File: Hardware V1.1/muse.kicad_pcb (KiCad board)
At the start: 2 copper layers, 71.6 x 61.5 mm, 53 parts, among them P1 3.5mm_line, P2 3.5mm_line, P3 RCA, P4 RCA, P8 ATX_PS_ON, P9 LED_Signal, Q1 FQP30N06L, Q2 FQP30N06L, Q3 FQP30N06L, Q4 FQP30N06L, Q5 FQP30N06L, Q6 FQP30N06L, SW1 PWR_SW, U1 MSGEQ7, U2 MSGEQ7, U3 74LS595, U4 Spark_Core

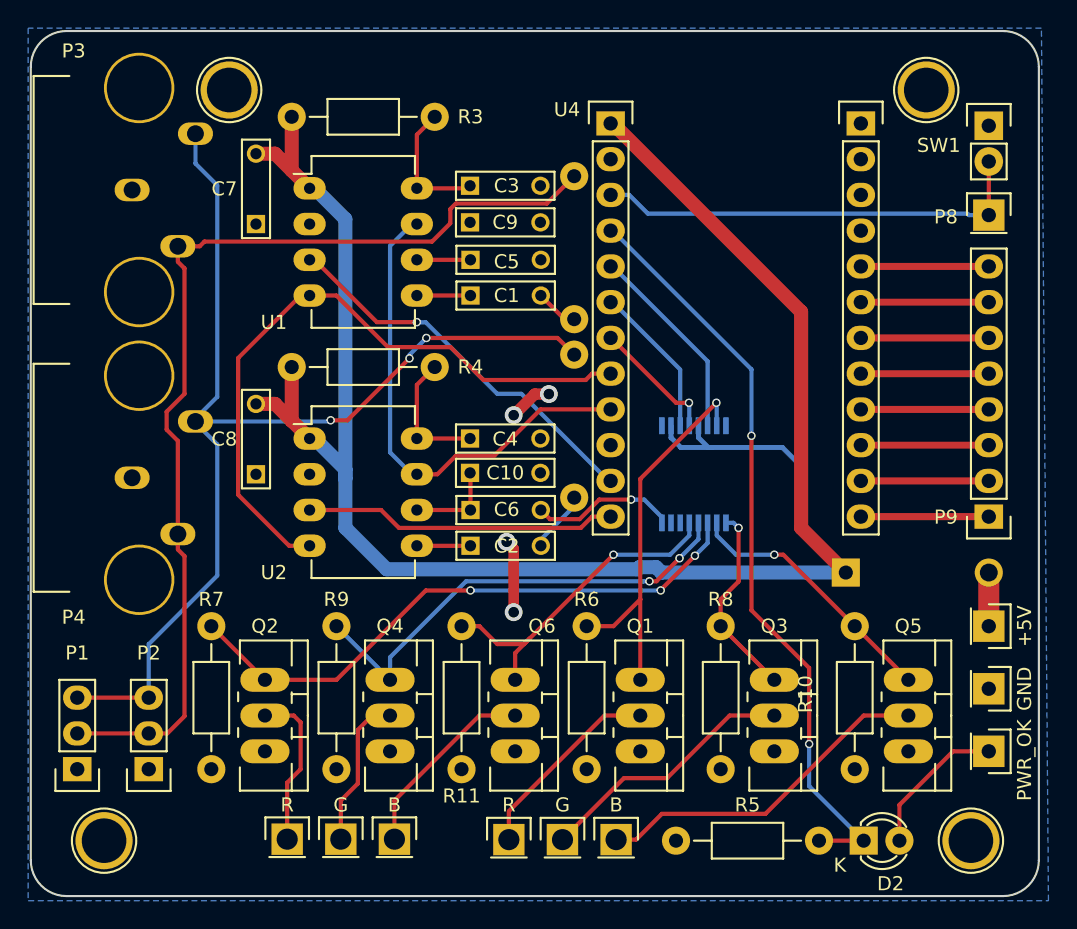
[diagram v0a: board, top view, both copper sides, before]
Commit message: Changed versioning scheme. Fixed problems and reuploaded to oshpark
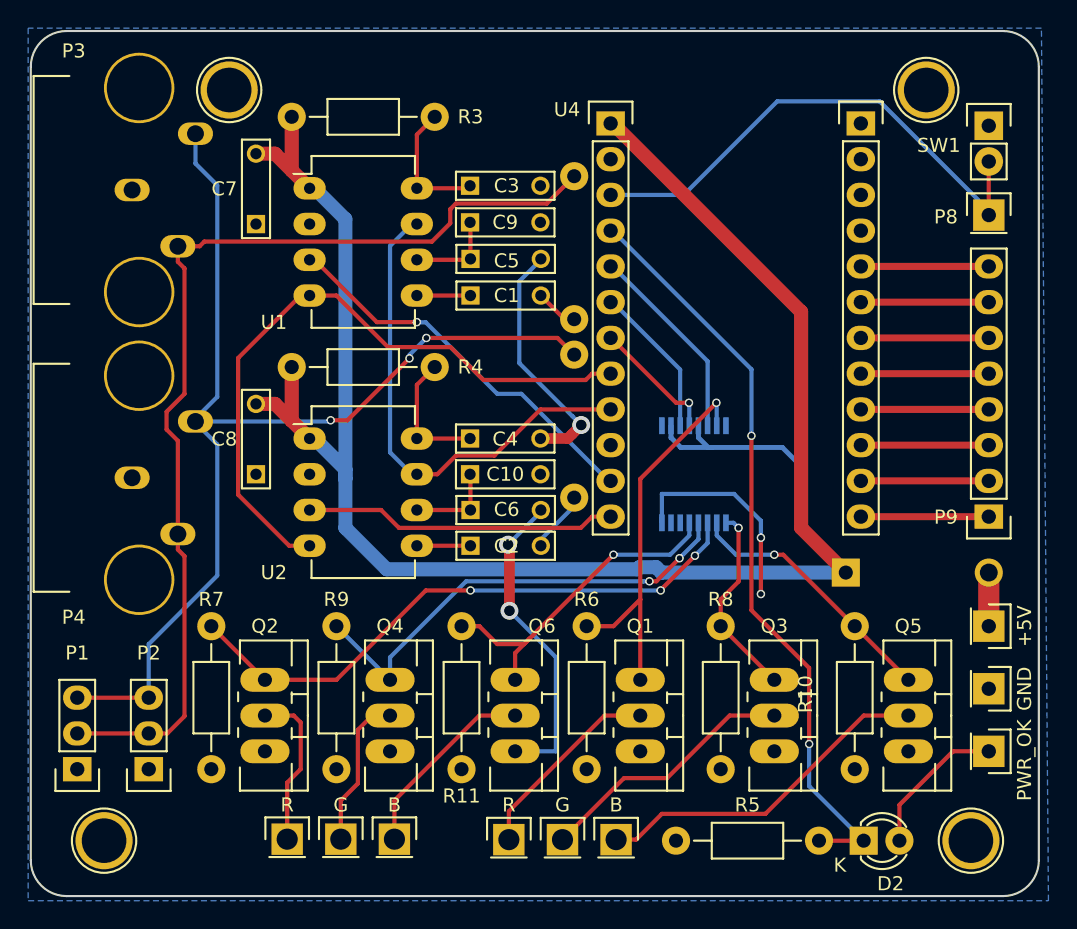
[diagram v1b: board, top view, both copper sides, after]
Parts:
- moved C10 0.10 mm to (114.9, 102.2)
- moved C5 0.06 mm to (114.9, 86.9)
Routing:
- net GND: track 10.4 -> 55.4 mm, vias 1 -> 5
- net (no net): track 8.33 -> 0.00 mm, vias 4 -> 0
- net /ATX_PWR_ON: track 27.5 -> 33.2 mm
- net Net-(C5-Pad1): track 3.81 -> 6.48 mm
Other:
- board text added: "(1.1)"
- board text removed: "(2.0)"
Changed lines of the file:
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@@
   (general
     (links 100)
-    (no_connects 3)
-    (area 82.434286 70.663999 156.111429 133.055)
+    (no_connects 1)
+    (area 82.434286 70.535 156.111429 133.055)
     (thickness 1.6)
     (drawings 11)
-    (tracks 275)
+    (tracks 285)
     (zones 0)
     (modules 53)
@@
     (aux_axis_origin 0 0)
     (grid_origin 103.505 89.535)
-    (visible_elements FFFFFF7F)
+    (visible_elements 7FFFFFFF)
     (pcbplotparams
-      (layerselection 0x00030_80000001)
+      (layerselection 0x010f0_80000001)
       (usegerberextensions false)
       (excludeedgelayer true)
@@
       (outputformat 1)
       (mirror false)
-      (drillshape 1)
+      (drillshape 0)
       (scaleselection 1)
-      (outputdirectory ""))
+      (outputdirectory Gerbers/))
   )
   (net 0 "")
@@
   )
   (module Capacitors_ThroughHole:C_Rect_L7_W2_P5 (layer F.Cu)
-    (at 114.935 86.995)
+    (at 114.935 86.9315)
     (descr "Film Capacitor Length 7 x Width 2mm, Pitch 5mm")
     (tags Capacitor)
@@
     (descr "Resistor, Axial,  RM 10mm, 1/3W,")
     (tags "Resistor, Axial, RM 10mm, 1/3W,")
-    (fp_text reference R1 (at 0 2.54 90) (layer B.SilkS)
+    (fp_text reference R1 (at 8.03 -0.1945 90) (layer B.SilkS)
       (effects (font (size 1 1) (thickness 0.15)) (justify mirror))
     )
@@
     (descr "Resistor, Axial,  RM 10mm, 1/3W,")
     (tags "Resistor, Axial, RM 10mm, 1/3W,")
-    (fp_text reference R2 (at 0 2.54 270) (layer B.SilkS)
+    (fp_text reference R2 (at 7.611 0.004 270) (layer B.SilkS)
       (effects (font (size 1 1) (thickness 0.15)) (justify mirror))
     )
@@
   )
   (module Capacitors_ThroughHole:C_Rect_L7_W2_P5 (layer F.Cu)
-    (at 114.905 102.135)
+    (at 114.905 102.235)
     (descr "Film Capacitor Length 7 x Width 2mm, Pitch 5mm")
     (tags Capacitor)
@@
     )
   )
-  (gr_text "(2.0)" (at 145.923 94.234 90) (layer B.SilkS)
+  (gr_text "(1.1)" (at 145.923 94.234 90) (layer B.SilkS)
     (effects (font (size 1 1) (thickness 0.2)) (justify left mirror))
   )
@@
   (gr_line (start 155.321 73.279) (end 155.321 129.667) (layer Edge.Cuts) (width 0.15))
   (gr_line (start 86.233 70.739) (end 152.781 70.739) (layer Edge.Cuts) (width 0.15))
-  (segment (start 118.005 112.035) (end 118.005 107.535) (width 0.762) (layer F.Cu) (net 0))
-  (via (at 117.505 107.035) (size 1.27) (drill 0.762) (layers F.Cu B.Cu) (net 0))
-  (segment (start 118.005 107.535) (end 117.505 107.035) (width 0.762) (layer F.Cu) (net 0))
-  (via (at 118.005 112.035) (size 1.27) (drill 0.762) (layers F.Cu B.Cu) (net 0))
-  (segment (start 118.005 98.035) (end 119.505 96.535) (width 0.808) (layer F.Cu) (net 0))
-  (segment (start 119.505 96.535) (end 120.505 96.535) (width 0.808) (layer F.Cu) (net 0))
-  (via (at 120.505 96.535) (size 1.27) (drill 0.762) (layers F.Cu B.Cu) (net 0))
-  (via (at 118.005 98.035) (size 1.27) (drill 0.762) (layers F.Cu B.Cu) (net 0))
   (segment (start 114.935 89.535) (end 111.125 89.535) (width 0.3) (layer F.Cu) (net 1) (status 30))
   (segment (start 119.935 89.535) (end 121.615 91.215) (width 0.3) (layer F.Cu) (net 2))
@@
   (segment (start 111.125 78.105) (end 112.395 76.835) (width 0.3) (layer F.Cu) (net 5) (status 20))
   (segment (start 111.125 81.915) (end 111.125 78.105) (width 0.3) (layer F.Cu) (net 5) (status 10))
-  (segment (start 126.34999 104.035) (end 127.285 104.035) (width 0.3) (layer B.Cu) (net 6))
-  (segment (start 127.285 104.035) (end 128.535 105.285) (width 0.3) (layer B.Cu) (net 6))
+  (segment (start 128.535 105.685) (end 128.535 103.632) (width 0.3) (layer B.Cu) (net 6))
+  (segment (start 128.535 103.632) (end 133.6675 103.632) (width 0.3) (layer B.Cu) (net 6))
+  (segment (start 133.6675 103.632) (end 135.5725 105.537) (width 0.3) (layer B.Cu) (net 6))
+  (segment (start 135.5725 105.537) (end 135.5725 106.7435) (width 0.3) (layer B.Cu) (net 6))
+  (segment (start 135.5725 106.7435) (end 135.5725 110.744) (width 0.3) (layer F.Cu) (net 6))
+  (via (at 135.5725 110.744) (size 0.6) (drill 0.4) (layers F.Cu B.Cu) (net 6))
+  (via (at 135.5725 106.7435) (size 0.6) (drill 0.4) (layers F.Cu B.Cu) (net 6))
+  (segment (start 119.905 99.695) (end 121.845 99.695) (width 0.762) (layer F.Cu) (net 6))
+  (segment (start 122.170001 99.369999) (end 122.805 98.735) (width 0.762) (layer F.Cu) (net 6))
+  (segment (start 122.170001 98.100001) (end 122.805 98.735) (width 0.3) (layer B.Cu) (net 6))
+  (segment (start 121.845 99.695) (end 122.170001 99.369999) (width 0.762) (layer F.Cu) (net 6))
+  (segment (start 118.405 94.335) (end 122.170001 98.100001) (width 0.3) (layer B.Cu) (net 6))
+  (segment (start 118.405 88.525) (end 118.405 94.335) (width 0.3) (layer B.Cu) (net 6))
+  (segment (start 119.935 86.995) (end 118.405 88.525) (width 0.3) (layer B.Cu) (net 6))
+  (via (at 122.805 98.735) (size 1.27) (drill 0.762) (layers F.Cu B.Cu) (net 6))
+  (segment (start 118.11 121.92) (end 121.005 121.92) (width 0.3) (layer B.Cu) (net 6))
+  (segment (start 121.005 121.92) (end 121.005 115.235) (width 0.3) (layer B.Cu) (net 6))
+  (segment (start 121.005 115.235) (end 117.705 111.935) (width 0.3) (layer B.Cu) (net 6))
+  (segment (start 117.605 107.235) (end 119.935 104.905) (width 0.3) (layer B.Cu) (net 6))
+  (segment (start 119.935 104.905) (end 119.935 104.775) (width 0.3) (layer B.Cu) (net 6))
+  (segment (start 117.705 111.935) (end 117.705 107.335) (width 0.762) (layer F.Cu) (net 6))
+  (segment (start 117.705 107.335) (end 117.605 107.235) (width 0.762) (layer F.Cu) (net 6))
+  (via (at 117.605 107.235) (size 1.27) (drill 0.762) (layers F.Cu B.Cu) (net 6))
+  (via (at 117.705 111.935) (size 1.27) (drill 0.762) (layers F.Cu B.Cu) (net 6))
   (segment (start 128.535 105.285) (end 128.535 105.685) (width 0.3) (layer B.Cu) (net 6))
-  (segment (start 119.935 104.775) (end 120.584999 105.424999) (width 0.3) (layer F.Cu) (net 6))
-  (segment (start 120.584999 105.424999) (end 122.691971 105.424999) (width 0.3) (layer F.Cu) (net 6))
-  (segment (start 122.691971 105.424999) (end 124.084852 104.032118) (width 0.3) (layer F.Cu) (net 6))
-  (segment (start 124.084852 104.032118) (end 126.347108 104.032118) (width 0.3) (layer F.Cu) (net 6))
-  (segment (start 126.347108 104.032118) (end 126.34999 104.035) (width 0.3) (layer F.Cu) (net 6))
-  (via (at 126.34999 104.035) (size 0.6) (drill 0.4) (layers F.Cu B.Cu) (net 6))
   (segment (start 111.125 99.695) (end 115.015 99.695) (width 0.3) (layer F.Cu) (net 7) (status 30))
   (segment (start 111.125 95.885) (end 112.395 94.615) (width 0.3) (layer F.Cu) (net 7) (status 20))
   (segment (start 111.125 99.695) (end 111.125 95.885) (width 0.3) (layer F.Cu) (net 7) (status 10))
+  (segment (start 114.935 86.995) (end 114.935 84.365) (width 0.3) (layer F.Cu) (net 8))
+  (segment (start 114.935 84.365) (end 114.905 84.335) (width 0.3) (layer F.Cu) (net 8))
   (segment (start 114.935 86.995) (end 111.125 86.995) (width 0.3) (layer F.Cu) (net 8) (status 30))
   (segment (start 103.855 99.695) (end 103.505 99.695) (width 1) (layer F.Cu) (net 9) (status 30))
@@
   (segment (start 134.9 94.778966) (end 134.9 99.5) (width 0.3) (layer B.Cu) (net 43))
   (via (at 134.9 99.5) (size 0.6) (drill 0.4) (layers F.Cu B.Cu) (net 43))
-  (segment (start 124.894362 82.385728) (end 126.210362 82.385728) (width 0.3) (layer B.Cu) (net 44))
-  (segment (start 126.210362 82.385728) (end 127.536752 83.712118) (width 0.3) (layer B.Cu) (net 44))
-  (segment (start 127.536752 83.712118) (end 150.239518 83.712118) (width 0.3) (layer B.Cu) (net 44))
-  (segment (start 150.239518 83.712118) (end 150.3474 83.82) (width 0.3) (layer B.Cu) (net 44))
-  (segment (start 150.3474 83.82) (end 151.765 83.82) (width 0.3) (layer B.Cu) (net 44))
+  (segment (start 124.894362 82.385728) (end 130.085272 82.385728) (width 0.3) (layer B.Cu) (net 44))
+  (segment (start 144.005 75.735) (end 151.765 83.495) (width 0.3) (layer B.Cu) (net 44))
+  (segment (start 130.085272 82.385728) (end 136.736 75.735) (width 0.3) (layer B.Cu) (net 44))
+  (segment (start 136.736 75.735) (end 144.005 75.735) (width 0.3) (layer B.Cu) (net 44))
+  (segment (start 151.765 83.495) (end 151.765 83.82) (width 0.3) (layer B.Cu) (net 44))
   (zone (net 6) (net_name GND) (layer B.Cu) (hatch edge 0.508)
     (connect_pads (clearance 0.508))
